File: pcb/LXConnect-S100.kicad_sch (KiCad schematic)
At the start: 16 parts, among them J1 LX, J11 CAN, J2 VP, J3 IN1, J4 IN2, J5 IN3, J6 IN4, J7 OAT, J8 SC, J9 PWR

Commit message: pcb: docu on board
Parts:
- JP1: value TERM -> CAN-TERMINATOR
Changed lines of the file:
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@@
 			)
 		)
-		(property "Value" "TERM"
+		(property "Value" "CAN-TERMINATOR"
 			(at 187.96 109.2199 90)
 			(effects

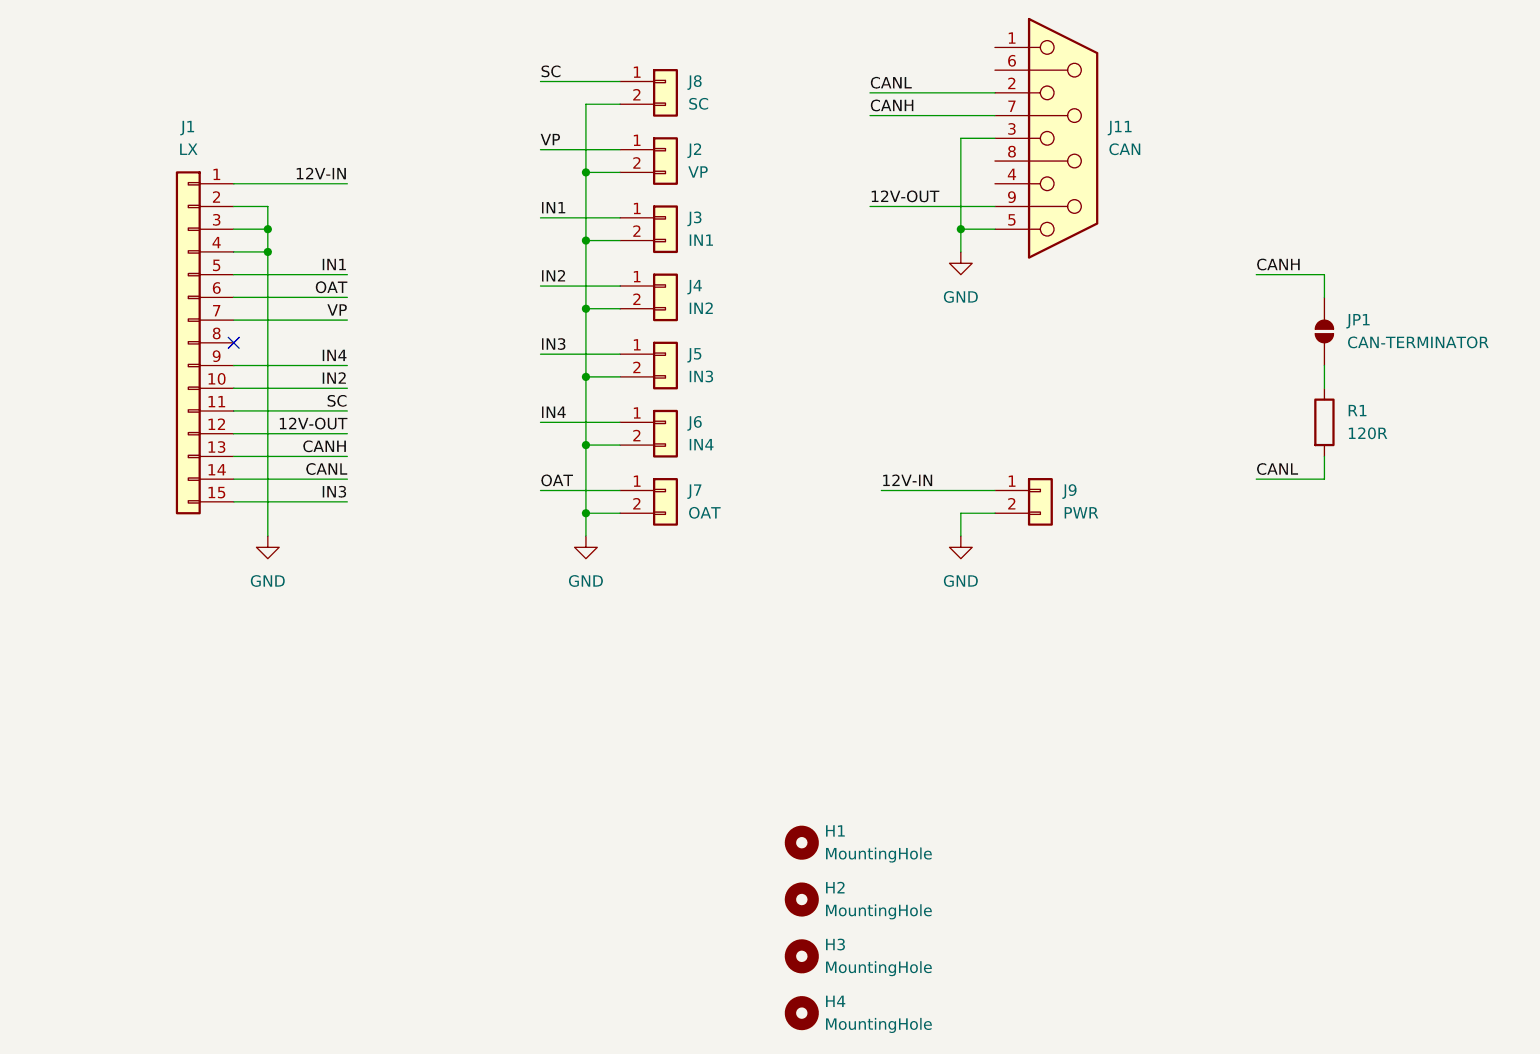
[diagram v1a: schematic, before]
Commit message: change connector to S100 to socket type to avoid shorts when not plugged
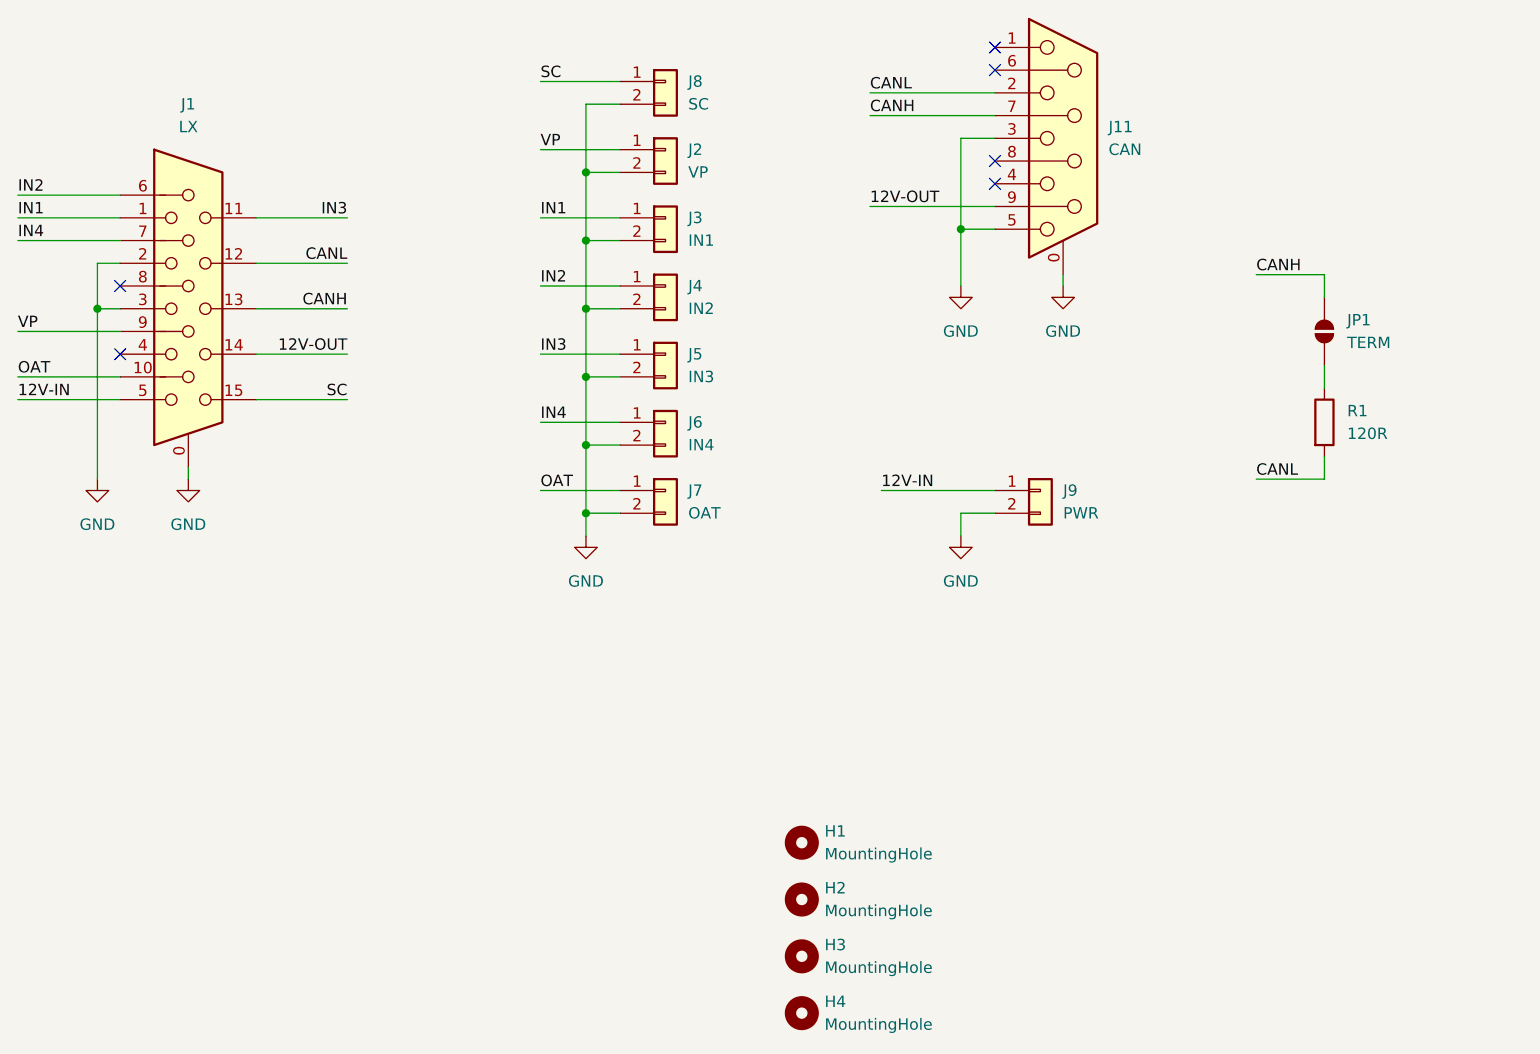
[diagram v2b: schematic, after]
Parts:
- removed J1: LX, Connector_Dsub:DSUB-15-HD_Male_Vertical_P2.29x1.98mm_MountingHoles, symbol Connector_Generic:Conn_01x15
- added J1: LX, Connector_Dsub:DSUB-15-HD_Socket_Vertical_P2.29x1.98mm_MountingHoles, symbol Connector:DE15_Socket_HighDensity_MountingHoles
- J11: footprint Connector_Dsub:DSUB-9_Female_Vertical_P2.77x2.84mm_MountingHoles -> Connector_Dsub:DSUB-9_Socket_Vertical_P2.77x2.84mm_MountingHoles; symbol Connector:DE9_Receptacle -> Connector:DE9_Socket_MountingHoles
- JP1: value CAN-TERMINATOR -> TERM
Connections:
- net 12V-IN: now also J1.5
- net 12V-OUT: now also J1.14
- net CANH: now also J1.13
- net CANL: now also J1.12
- net GND: now also J11.0 (PAD), J1.0, J1.2, J1.3
- net IN1: now also J1.1
- net IN2: now also J1.6
- net IN3: now also J1.11
- net IN4: now also J1.7
- net OAT: now also J1.10
- net SC: now also J1.15
- net VP: now also J1.9
- no-connect marks 1 -> 6
